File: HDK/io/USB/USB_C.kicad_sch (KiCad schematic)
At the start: 9 parts, among them J101 USB_C, U101 USBLC6-2SC6

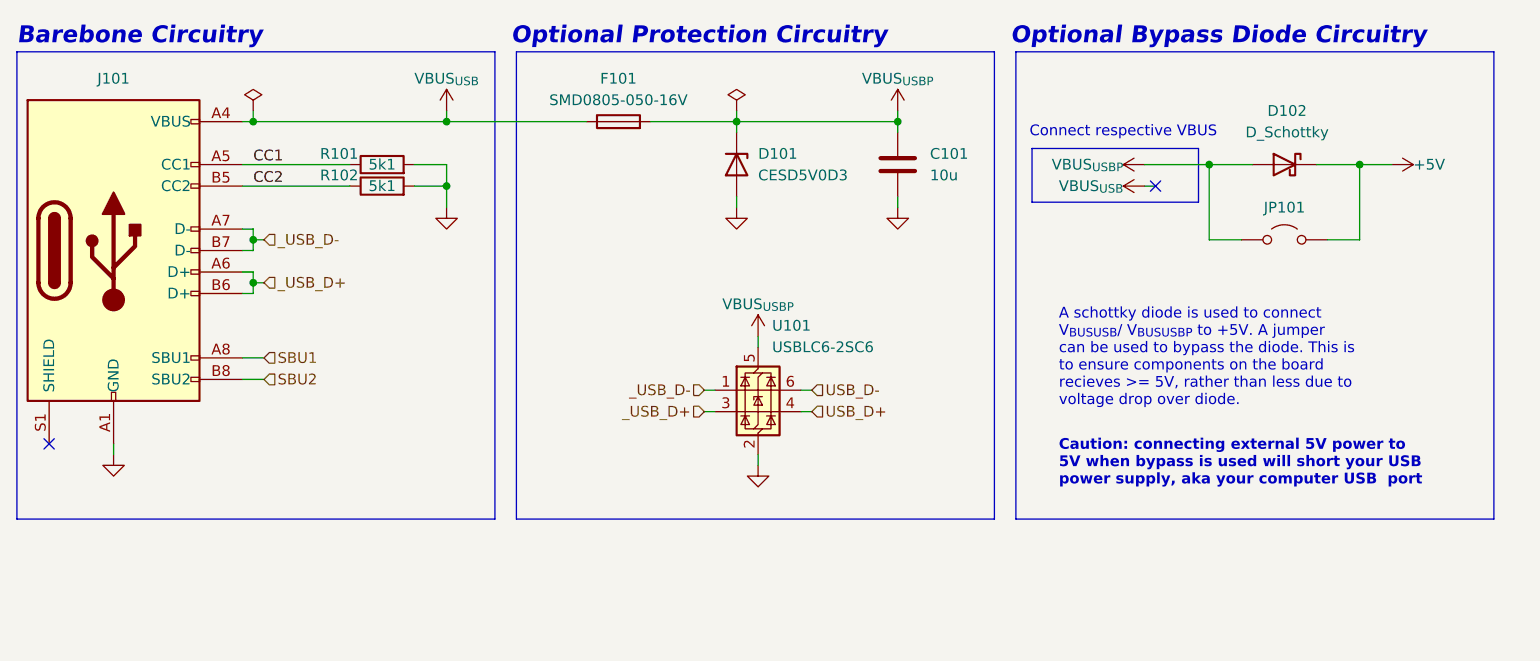
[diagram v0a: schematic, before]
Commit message: update gitignore
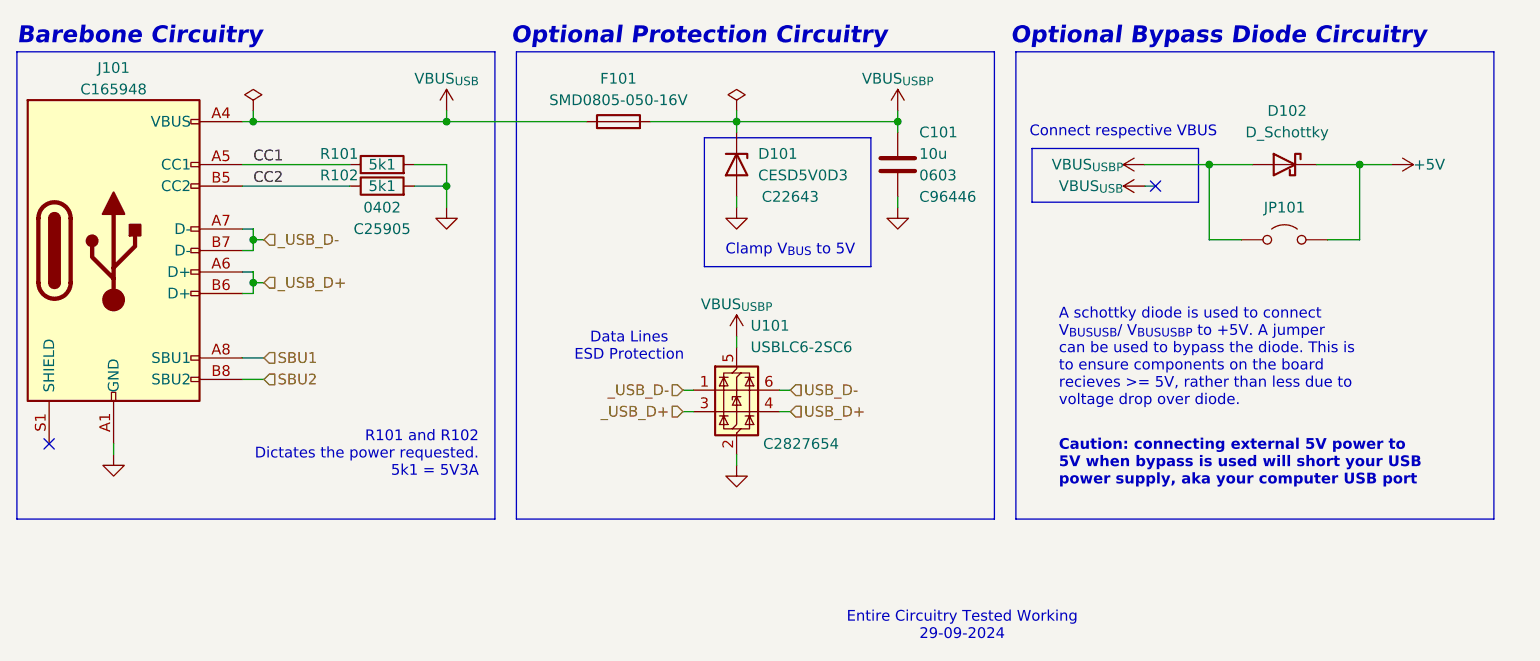
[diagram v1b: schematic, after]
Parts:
- removed C101: 10u, symbol scottcjx-common-parts:10uF
- removed J101: USB_C, NVF-Kicad:USBC_HRO_TYPE-C-31-M-12, symbol Connector:USB_C_Receptacle_USB2.0
- removed R101, R102: 5k1, Resistor_SMD:R_0603_1608Metric, symbol Device:R
- added C101: 10u, Capacitor_SMD:C_0603_1608Metric, symbol scottcjx-common-parts:10uF_0603
- added J101: USB_C_Receptacle_USB2.0_16P, Connector_USB:USB_C_Receptacle_HRO_TYPE-C-31-M-12, symbol scottcjx-common-parts:USB_C_16P
- added R101, R102: 5k1, Resistor_SMD:R_0402_1005Metric, symbol scottcjx-common-parts:5k1Ω_0402
- D101: LCSC (none) -> C22643
- U101: LCSC (none) -> C2827654
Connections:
- net CC1: now also J101.A5 (CC1), R101.1
- net CC2: now also J101.B5 (CC2), R102.1
- net GND: now also C101.2, J101.A1 (GND), J101.A12 (GND), J101.B1 (GND), J101.B12 (GND), R101.2, R102.2
- net SBU1: now also J101.A8 (SBU1)
- net SBU2: now also J101.B8 (SBU2)
- net VBUS_{USBP}: now also C101.1
- net VBUS_{USB}: now also J101.A4 (VBUS), J101.A9 (VBUS), J101.B4 (VBUS), J101.B9 (VBUS)
- net _USB_D+: now also J101.A6 (D+), J101.B6 (D+)
- net _USB_D-: now also J101.A7 (D-), J101.B7 (D-)
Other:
- note added: "Clamp V_{BUS} to 5V"
- note added: "Data Lines ESD Protection"
- note added: "Entire Circuitry Tested Working 29-09-2024"
- note added: "R101 and R102 Dictates the power requested. 5k1 = 5V3A"
- moved on the sheet: U101
